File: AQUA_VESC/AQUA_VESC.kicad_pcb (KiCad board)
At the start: 2 copper layers, 101.5 x 77.8 mm, 224 parts, among them J1 Conn_01x06_Pin, J2 Conn_01x02_Pin, J3 Conn_01x05_Pin, M1 Motor_Servo_Hitec, Q1 TK3R2E06PL, Q10 AO3400A, Q11 AO3401A, Q12 AO3400A, Q13 AO3401A, Q2 TK3R2E06PL, Q3 TK3R2E06PL, Q4 TK3R2E06PL, Q5 TK3R2E06PL, Q6 TK3R2E06PL, Q7 AO3400A, Q8 AO3400A, Q9 AO3401A, U1 SMF05CT1G, U10 22uH, U11 MX27524ES, U12 TP2604-SR, U3 STM32F405RGTx, U4 TJA1051T-3, U5 TP2604-SR, U6 DRV8301QDCAQ1, U7 22uH, U8 AMS1117-3.3, U9 LMR16030SDDAR, X1 8MHz

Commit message: 制御基板REV01完成
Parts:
- removed the C60 at (52.5, 43.5)
- removed the C61 at (64.8, 41.2)
- removed the C62 at (50.2, 35.5)
- removed CAN1, CAN2: Conn_01x02_Pin, Connector_JST:JST_XA_S02B-XASK-1_1x02_P2.50mm_Horizontal
- removed D5, SERVO_CNT1: EMERALD, LED_SMD:LED_0805_2012Metric
- removed D6: SS36, Diode_SMD:D_SMA
- removed the J2 at (69.2, 88.8)
- removed the Q10 at (134.1, 38.0)
- removed the Q12 at (127.0, 38.0)
- removed the Q8 at (130.6, 38.0)
- removed the R1 at (53.8, 30.2)
- removed the R69 at (55.0, 42.8)
- removed the R70 at (57.8, 47.2)
- removed the R71 at (63.0, 46.5)
- removed the R72 at (55.0, 45.8)
- removed the R73 at (64.0, 44.2)
- removed R79: 1k, Resistor_SMD:R_0603_1608Metric
- removed R82: 56k, Resistor_SMD:R_0603_1608Metric
- removed R83: 12k, Resistor_SMD:R_0603_1608Metric
- removed U12: TP2604-SR, specific_footprint_library:SO-8SOIC-8_TPK
- removed the U9 at (59.5, 43.0)
- added 6V_OK1: YELLOW, LED_SMD:LED_0805_2012Metric, F.Cu at (159.4, 57.2)
- added C65: 4.7u, 100V, Capacitor_SMD:C_1210_3225Metric, F.Cu at (62.8, 41.4)
- added C68: 4.7u, 100V, Capacitor_SMD:C_1210_3225Metric, F.Cu at (31.1, 14.2)
- added C69: 2.2u, Capacitor_SMD:C_0603_1608Metric, F.Cu at (35.9, 13.3)
- added C70: 13p, Capacitor_SMD:C_0603_1608Metric, F.Cu at (35.9, 15.8)
- added C71: 0.47u, Capacitor_SMD:C_0603_1608Metric, F.Cu at (35.9, 18.3)
- added C72: 22u, Capacitor_SMD:C_1210_3225Metric, F.Cu at (31.1, 18.4)
- added C73: 22u, Capacitor_SMD:C_1210_3225Metric, F.Cu at (52.0, 36.5)
- added Q11: 2N7002, Package_TO_SOT_SMD:SOT-23, F.Cu at (128.0, 39.4)
- added Q13: 2N7002, Package_TO_SOT_SMD:SOT-23, F.Cu at (159.7, 53.5)
- added Q9: 2N7002, Package_TO_SOT_SMD:SOT-23, F.Cu at (135.0, 39.4)
- added U11: 15uH, specific_footprint_library:IND-SMD_L7.1-W6.6, F.Cu at (38.4, 28.5)
- C63, C64: value 22u -> 4.7u, 100V
- C66: value 1n -> 4.7u, 100V; footprint Capacitor_SMD:C_0603_1608Metric -> Capacitor_SMD:C_1210_3225Metric
- C67: value 100n -> 4.7u, 100V; footprint Capacitor_SMD:C_0603_1608Metric -> Capacitor_SMD:C_1210_3225Metric
- J1: value Conn_01x06_Pin -> Conn_01x12_Socket; footprint Connector_JST:JST_XA_S06B-XASK-1_1x06_P2.50mm_Horizontal -> Connector_PinSocket_2.54mm:PinSocket_1x12_P2.54mm_Horizontal
- M1: footprint Connector_JST:JST_XA_S03B-XASK-1N-BN_1x03_P2.50mm_Horizontal -> Connector_PinSocket_2.54mm:PinSocket_1x03_P2.54mm_Horizontal
- Q7: value AO3400A -> 2N7002
- R74: value 2.2k -> 390
- R75: value 150k -> 51k
- R76: value 18k -> 100k
- R77: value SL1TTE5L00F -> 82k; footprint specific_footprint_library:RES_SL1TTE5L00F_KOA -> Resistor_SMD:R_0603_1608Metric
- R78: value 1k -> 15k
- R80: value 1k -> 20k
- R81: value 200k -> 100k
- RGBLED1: footprint Connector_JST:JST_XA_S04B-XASK-1N-BN_1x04_P2.50mm_Horizontal -> Connector_PinSocket_2.54mm:PinSocket_1x04_P2.54mm_Horizontal
- U10: value 22uH -> LM76002; footprint specific_footprint_library:IND-SMD_L7.0-W6.6 -> Package_DFN_QFN:Texas_RNP0030B_WQFN-30-1EP_4x6mm_P0.5mm_EP1.8x4.5mm_ThermalVias
- moved Q7 68.9 mm to (131.5, 39.4), turned to 90 degrees
- moved R76 38.8 mm to (39.9, 13.3)
- moved R74 36.3 mm to (35.9, 20.9)
- moved R77 26.8 mm to (39.9, 15.8), turned to 0 degrees
- moved R75 25.1 mm to (35.9, 23.4), turned to 0 degrees
- moved R78 23.0 mm to (39.9, 18.3), turned to 0 degrees
- moved C67 21.3 mm to (62.8, 47.8), turned to 0 degrees
- moved R81 20.3 mm to (39.9, 23.4), turned to 0 degrees
- moved R80 18.3 mm to (39.9, 20.9)
- moved J1 18.2 mm to (78.5, 78.2), turned to 90 degrees
- moved C66 18.2 mm to (62.8, 44.6), turned to 0 degrees
- moved C63 17.0 mm to (62.0, 26.5), turned to 0 degrees
- moved C64 16.0 mm to (58.8, 50.1), turned to -90 degrees
- moved U10 7.69 mm to (57.8, 44.0), turned to 0 degrees
- moved R49 4.60 mm to (92.8, 56.0), turned to 90 degrees
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- renumbered C68 to C56, C69 to C57, C56 to C58, C57 to C59, C58 to C60, C59 to C61, C65 to C62, J3 to J2, JP2 to JP1, JP1 to JP2, Q11 to Q10, Q13 to Q12, Q9 to Q8, R2 to R1, R11 to R10, R12 to R11, R13 to R12, R14 to R13, R15 to R14, R16 to R15, R17 to R16, R18 to R17, R19 to R18, R20 to R19, R3 to R2, R21 to R20, R22 to R21, R23 to R22, R24 to R23, R25 to R24, R26 to R25, R27 to R26, R28 to R27, R29 to R28, R30 to R29, R4 to R3, R31 to R30, R32 to R31, R33 to R32, R34 to R33, R35 to R34, R36 to R35, R37 to R36, R38 to R37, R39 to R38, R40 to R39, R5 to R4, R41 to R40, R42 to R41, R43 to R42, R44 to R43, R45 to R44, R46 to R45, R47 to R46, R48 to R47, R49 to R48, R50 to R49, R6 to R5, R51 to R50, R52 to R51, R53 to R52, R54 to R53, R55 to R54, R56 to R55, R57 to R56, R58 to R57, R59 to R58, R60 to R59, R7 to R6, R61 to R60, R62 to R61, R63 to R62, R64 to R63, R65 to R64, R66 to R65, R67 to R66, R68 to R67, R84 to R68, R85 to R69, R8 to R7, R86 to R70, R87 to R71, R88 to R72, R89 to R73, R9 to R8, R10 to R9, U11 to U9
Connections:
- C62 pad 1: +7V -> +6V
- C63 pad 1: +7V -> V_SUPPLY
- C64 pad 1: +7V -> V_SUPPLY
- C66 pad 1: Net-(M1--) -> V_SUPPLY
- C67 pad 1: +7V -> V_SUPPLY
- J1 pad 1: GNDD -> +5V
- J1 pad 2: /STM32F405/HALL_1 -> /CAN/CANH
- J1 pad 3: /STM32F405/HALL_2 -> /CAN/CANL
- J1 pad 4: /STM32F405/HALL_3 -> GNDD
- J1 pad 5: /STM32F405/TEMP_MOTER -> /CAN/CANH
- J1 pad 6: +3V3 -> /CAN/CANL
- M1 pad 2: +7V -> +6V
- M1 pad 3: Net-(M1--) -> GNDPWR
- Q7 pad 1: Net-(Q7-G) -> /RGBLED_Driver/RED_GATE
- Q7 pad 3: Net-(D5-K) -> Net-(Q7-D)
- Q8 pad 1: Net-(Q8-D) -> Net-(Q7-D)
- R69 pad 1: Net-(Q8-D) -> Net-(Q7-D)
- R74 pad 1: Net-(D5-A) -> +6V
- R74 pad 2: +7V -> Net-(6V_OK1-A)
- R75 pad 1: Net-(U9-FB) -> +6V
- R75 pad 2: +7V -> Net-(Q13-G)
- R76 pad 1: GNDPWR -> V_SUPPLY
- R76 pad 2: Net-(U9-FB) -> Net-(U10-EN)
- R77 pad 2: Net-(M1--) -> Net-(U10-RT)
- R78 pad 1: Net-(M1--) -> Net-(U10-EN)
- R78 pad 2: Net-(U12--INA) -> GNDPWR
- R80 pad 1: SERVO_CURRENT -> Net-(U10-FB)
- R80 pad 2: Net-(U12-OUTA) -> GNDPWR
- R81 pad 1: Net-(U12--INA) -> Net-(U10-FB)
- R81 pad 2: Net-(U12-OUTA) -> +6V
- U10 pad 1: Net-(D6-K) -> Net-(U10-SW-Pad1)
- U10 pad 2: +7V -> Net-(U10-SW-Pad1)
- U9 pad 6: +7V -> +6V
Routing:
- net +7V: track 33.0 -> 0.00 mm, vias 7 -> 0
- net Net-(M1-PWM): track 29.3 -> 0.99 mm, vias 2 -> 1
- net Net-(D6-K): track 14.3 -> 0.00 mm
- net Net-(U9-FB): track 12.4 -> 0.00 mm, vias 2 -> 0
- net +5V: track 201.9 -> 213.3 mm, vias 9 -> 12
- net Net-(M1--): track 10.8 -> 0.00 mm, vias 1 -> 0
- net Net-(Q7-D): track 0.00 -> 8.85 mm
- net Net-(Q8-D): track 8.85 -> 0.00 mm
- net Net-(U9-BOOT): track 8.53 -> 0.00 mm, vias 2 -> 0
- net Net-(U9-EN): track 8.49 -> 0.00 mm
- net Net-(U12--INB): track 7.75 -> 0.00 mm
- net SERVO_CURRENT: track 7.02 -> 0.00 mm
- net +3V3: track 69.2 -> 63.6 mm
- net /DRV8301/GL_B: track 22.7 -> 18.0 mm
- net /STM32F405/HALL_3: track 35.7 -> 40.3 mm
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- removed copper zone on F.Cu, net +7V
- removed copper zone on F.Cu, net Net-(D6-K)
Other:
- board size 101.5 x 77.8 mm -> 101.4 x 77.8 mm
- board text added: "5V"
- board text added: "H1"
- board text added: "H2"
- board text added: "H3"
- board text added: "L"
- board text added: "REV02"
- board text added: "T"
- board text added: "servo gpio-icu R gpio-tx G gpio-rx B gpio-hall1 ws gpio-adc"
- board text removed: "H L"
- board text removed: "HALL SENSOR"
- board text removed: "REV01"
- board text removed: "VESC_ID"

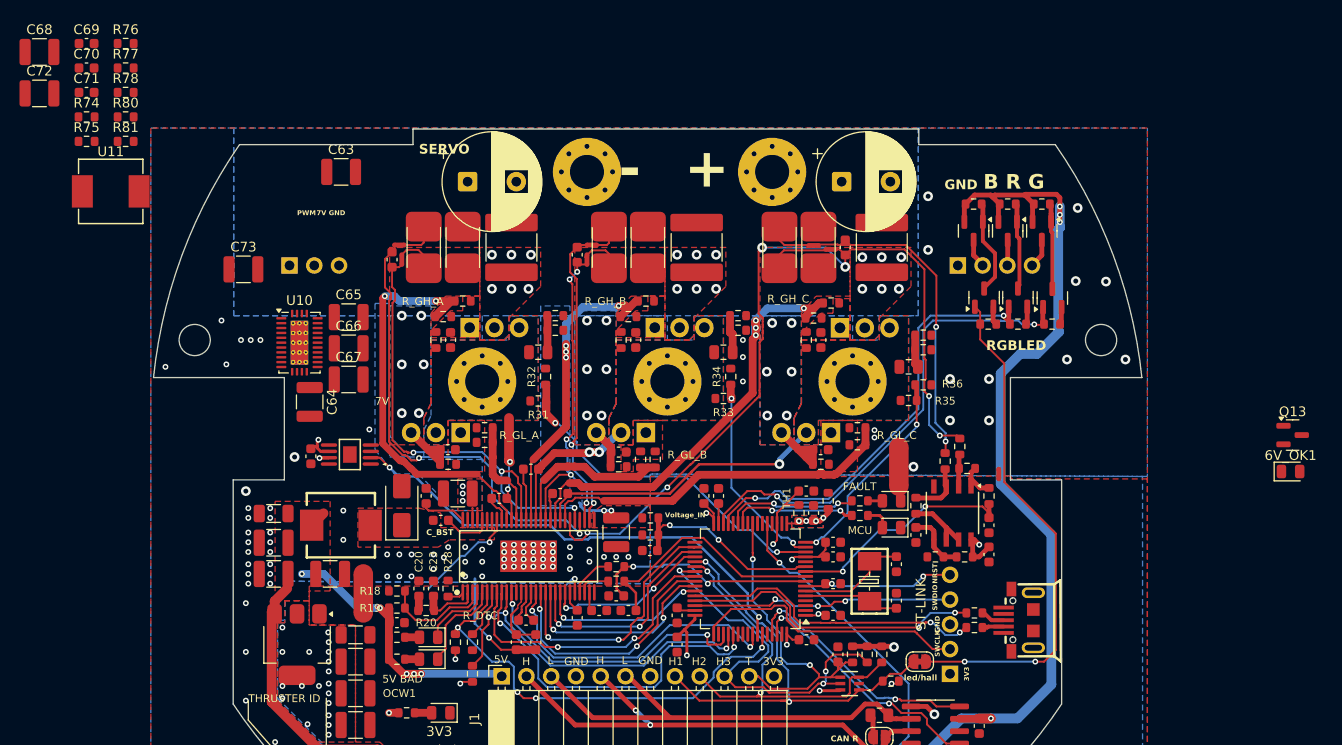
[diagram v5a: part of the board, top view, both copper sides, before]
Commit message: 方針変更、back_connector_escにMT60を使用しないことに
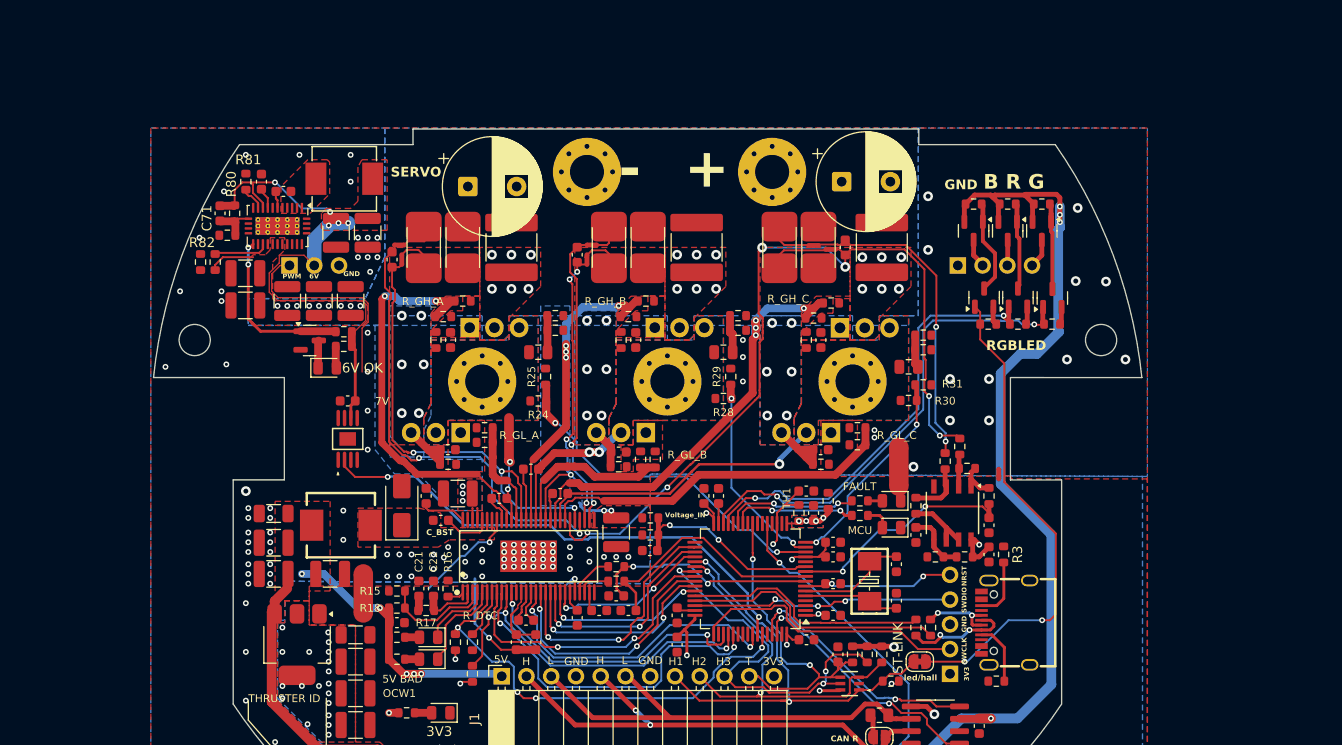
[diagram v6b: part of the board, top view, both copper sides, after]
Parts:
- removed the C68 at (31.1, 14.2)
- added R3: 5.1k, Resistor_SMD:R_0603_1608Metric, F.Cu at (130.0, 65.8)
- added R6: 5.1k, Resistor_SMD:R_0603_1608Metric, F.Cu at (129.2, 78.8)
- C71: renamed from C70; value 13p -> 12p
- USB1: value ~ -> TYPEC; footprint specific_footprint_library:MICRO-USB-SMD_5P-P0.65-H-F_MICRO5.9MMUSB -> specific_footprint_library:USB-C_SMD-TYPE-C-31-M-12
- moved Q13 101.3 mm to (58.8, 43.8)
- moved 6V_OK1 99.4 mm to (60.6, 46.6)
- moved C69 36.6 mm to (64.8, 32.8), turned to -90 degrees
- moved R76 35.4 mm to (62.3, 44.4), turned to 180 degrees
- moved R79 32.8 mm to (62.3, 42.9), turned to 180 degrees
- moved R77 24.2 mm to (49.1, 35.8), turned to 90 degrees
- moved U10 24.0 mm to (62.4, 27.2)
- moved C72 22.9 mm to (53.9, 27.5), turned to 90 degrees
- moved C68 22.6 mm to (56.1, 28.5)
- moved C71 20.2 mm to (49.6, 30.8), turned to 90 degrees
- moved R78 19.0 mm to (47.6, 35.8), turned to -90 degrees
- moved R81 17.0 mm to (52.2, 27.5), turned to -90 degrees
- moved R82 16.0 mm to (50.4, 33.0), turned to 180 degrees
- moved C63 14.3 mm to (52.2, 36.9), turned to 180 degrees
- moved R80 13.4 mm to (51.1, 30.8), turned to 90 degrees
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- renumbered C8 to C10, C3 to C11, C6 to C12, C5 to C13, C9 to C14, C39 to C16, C43 to C17, C44 to C18, C45 to C19, C46 to C20, C20 to C21, C23 to C22, C30 to C23, C37 to C24, C33 to C25, C38 to C26, C40 to C27, C41 to C28, C42 to C29, C4 to C3, C34 to C30, C25 to C31, C18 to C32, C19 to C33, C35 to C34, C36 to C35, C24 to C36, C31 to C37, C21 to C38, C22 to C39, C7 to C4, C32 to C40, C26 to C41, C29 to C42, C17 to C43, C27 to C44, C16 to C45, C28 to C46, C50 to C47, C51 to C48, C54 to C49, C10 to C5, C56 to C50, C57 to C51, C60 to C52, C47 to C53, C52 to C54, C58 to C55, C49 to C56, C55 to C57, C61 to C58, C48 to C59, C11 to C6, C53 to C60, C59 to C61, C71 to C68, C72 to C69, C12 to C7, C73 to C70, C69 to C72, C13 to C8, C14 to C9, H5 to H1, H1 to H2, H2 to H3, H3 to H4, H4 to H5, NT6 to NT5, NT8 to NT6, NT5 to NT7, NT7 to NT8, Q7 to Q10, Q9 to Q11, Q11 to Q12, Q3 to Q2, Q5 to Q3, Q2 to Q4, Q4 to Q5, Q8 to Q7, Q10 to Q8, Q12 to Q9, R8 to R10, R9 to R11, R10 to R12, R11 to R13, R12 to R14, R18 to R15, R28 to R16, R20 to R17, R19 to R18, R21 to R19, R3 to R2, R22 to R20, R17 to R21, R25 to R22, R31 to R24, R32 to R25, R33 to R28, R34 to R29, R35 to R30, R36 to R31, R15 to R32, R16 to R33, R29 to R34, R13 to R35, R14 to R36, R30 to R37, R24 to R38, R64 to R39, R6 to R4, R37 to R40, R47 to R41, R57 to R42, R38 to R43, R48 to R44, R58 to R45, R42 to R46, R52 to R47, R62 to R48, R39 to R49, R7 to R5, R49 to R50, R59 to R51, R40 to R52, R50 to R53, R60 to R54, R45 to R55, R46 to R56, R55 to R57, R56 to R58, R66 to R59, R67 to R60, R41 to R61, R51 to R62, R61 to R63, R43 to R64, R44 to R65, R53 to R66, R54 to R67, R63 to R68, R65 to R69, R2 to R7, R69 to R70, R73 to R72, R68 to R73, R70 to R74, R72 to R75, R74 to R76, R76 to R77, R75 to R79, R4 to R8, R81 to R80, R77 to R81, R80 to R82, R5 to R9, U11 to U10, U10 to U11, U8 to U5, U5 to U8
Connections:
- C68 pad 2: GNDPWR -> Net-(C68-Pad2)
- R4 pad 2: Net-(USB1-D-) -> USB_D-
- R5 pad 2: Net-(USB1-D+) -> USB_D+
- U10 pad 1: Net-(U10-SW-Pad1) -> Net-(C68-Pad2)
- U11 pad 1: Net-(U10-SW-Pad1) -> Net-(C68-Pad2)
- U11 pad 2: Net-(U10-SW-Pad1) -> Net-(C68-Pad2)
- U11 pad 3: Net-(U10-SW-Pad1) -> Net-(C68-Pad2)
- U11 pad 4: Net-(U10-SW-Pad1) -> Net-(C68-Pad2)
- U11 pad 5: Net-(U10-SW-Pad1) -> Net-(C68-Pad2)
- USB1 pad 1: unconnected-(USB1-VBUS-Pad1) -> GNDD
- USB1 pad 2: Net-(USB1-D-) -> GNDD
- USB1 pad 3: Net-(USB1-D+) -> GNDD
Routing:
- net +6V: track 3.06 -> 55.8 mm, vias 1 -> 5
- net Net-(M1-PWM): track 0.99 -> 21.7 mm, vias 1 -> 0
- net Net-(Q13-G): track 0.00 -> 17.8 mm, vias 0 -> 2
- net USB_D-: track 0.00 -> 11.0 mm, vias 0 -> 2
- net USB_D+: track 0.00 -> 7.54 mm, vias 0 -> 2
- net Net-(USB1-CC1): track 0.00 -> 6.35 mm
- net Net-(USB1-CC2): track 0.00 -> 6.05 mm
- net /STM32F405/USB_DM: track 31.3 -> 25.4 mm, vias 2 -> 0
- net Net-(U11-EN): track 0.00 -> 5.47 mm
- net V_SUPPLY: track 6.93 -> 11.7 mm, vias 23 -> 32
- net Net-(U11-FB): track 0.00 -> 4.50 mm
- net /STM32F405/USB_DP: track 31.4 -> 27.1 mm, vias 2 -> 0
- net /SERVO/SERVO_PWM: track 49.5 -> 52.5 mm
- net Net-(6V_OK1-K): track 0.00 -> 2.83 mm
- net Net-(U11-RT): track 0.00 -> 2.53 mm
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- added copper zone on F.Cu, net +6V
- added copper zone on F.Cu, net Net-(C68-Pad2)
- removed copper zone on F.Cu, net Net-(Q4-G)
- removed copper zone on B.Cu, net Net-(Q5-S)
- removed copper zone on F.Cu, net Net-(Q5-S)
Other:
- board text added: "6V"
- board text added: "6V OK"

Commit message: ESC周りの配線用基板進捗
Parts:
- C50, C51: footprint Capacitor_THT:CP_Radial_D10.0mm_P5.00mm -> specific_footprint_library:CP_Radial_D10.0mm_P5.00mm_nofill
- U2: footprint basic_parts:wetness sensor -> specific_footprint_library:wetness sensor
- moved U2 1.52 mm to (115.2, 98.0)
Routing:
- net Net-(M1-PWM): track 21.7 -> 42.4 mm
- net /STM32F405/ADC_EXT: track 36.0 -> 39.5 mm
- net Net-(U11-EN): track 5.47 -> 7.04 mm
- net BLUE_GATE: track 50.3 -> 49.8 mm
- net Net-(Q5-S): vias 0 -> 6
- net Net-(Q4-S): vias 12 -> 6
- net GNDPWR: vias 115 -> 119
- added copper zone on F.Cu, net Net-(Q4-G)
- added copper zone on B.Cu, net Net-(Q5-S)
- added copper zone on F.Cu, net Net-(Q5-S)
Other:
- board size 101.4 x 77.8 mm -> 101.4 x 77.7 mm
